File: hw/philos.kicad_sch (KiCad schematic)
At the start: 25 parts, among them SW2 Reset Button, U1 8086_Min_Mode, U11 71256SA25TPGI, U12 SN74LS161AN, U13 SN74AHC14N, U14 8259, U15 W27C512-45Z, U16 71256SA25TPGI, U17 8255, U18 MAX232N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

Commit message: hw: do some minor changes
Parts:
- removed R9: 1K ohm, symbol Device:R
- added RV1: R_Potentiometer, symbol Device:R_Potentiometer
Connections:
- net GND: now also RV1.1
- net VCC: now also RV1.3
- net indirizzi0: now also A2.D22; no longer A2.D2 (D2_INT0)
- net indirizzi1: now also A2.D23; no longer A2.D3 (D3_INT1)
- net indirizzi10: now also A2.D32; no longer A2.D12
- net indirizzi11: now also A2.D33; no longer A2.D13
- net indirizzi12: now also A2.D34; no longer A2.D22
- net indirizzi13: now also A2.D35; no longer A2.D23
- net indirizzi14: now also A2.D36; no longer A2.D24
- net indirizzi15: now also A2.D37; no longer A2.D25
- net indirizzi16: now also A2.D38; no longer A2.D26
- net indirizzi17: now also A2.D39; no longer A2.D27
- net indirizzi18: now also A2.D40; no longer A2.D28
- net indirizzi19: now also A2.D41; no longer A2.D29
- net indirizzi2: now also A2.D24; no longer A2.D4
- net indirizzi3: now also A2.D25; no longer A2.D5
- net indirizzi4: now also A2.D26; no longer A2.D6
- net indirizzi5: now also A2.D27; no longer A2.D7
- net indirizzi6: now also A2.D28; no longer A2.D8
- net indirizzi7: now also A2.D29; no longer A2.D9
- net indirizzi8: now also A2.D30; no longer A2.D10
- net indirizzi9: now also A2.D31; no longer A2.D11
- net at U5.20 (*CE): now also A2.D49; no longer A2.D37
- net at U14.1 (~{CS}): now also A2.D46; no longer A2.D34
- net at U11.20 (~{CS}), U16.20 (~{CS}): now also A2.D47; no longer A2.D35
- net at U1.28 (M/~{IO}): now also A2.D42; no longer A2.D30
- net at U7.11 (*CS): now also A2.D43; no longer A2.D31
- net at DS2.8 (E): now also A2.D44; no longer A2.D32
- net at U17.6 (~{CS}): now also A2.D45; no longer A2.D33
- net at U15.20 (*CE): now also A2.D48; no longer A2.D36
- net at DS2.5 (Vo): now also RV1.2

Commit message: hw: Add control bus pins on Arduino
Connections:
- net at U5.20 (*CE): now also A2.D52 (D52_SCK); no longer A2.D49
- net at U14.1 (~{CS}): now also A2.D49; no longer A2.D46
- net at U1.29 (~{WR}), U11.27 (~{WE}), U14.2 (~{WR})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: now also A2.D44
- net at U1.32 (~{RD}), U11.22 (~{OE}), U14.3 (~{RD})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: now also A2.D43
- net at U11.20 (~{CS}), U16.20 (~{CS}): now also A2.D50 (D50_MISO); no longer A2.D47
- net at A2.D42: now also U1.25 (ALE), U6.11 (LE), U8.11 (LE), U9.11 (LE); no longer U1.28 (M/~{IO})
- net at U7.11 (*CS): now also A2.D46; no longer A2.D43
- net at DS2.8 (E): now also A2.D47; no longer A2.D44
- net at A2.D45: now also U1.28 (M/~{IO}); no longer U17.6 (~{CS})
- net at A2.D48: now also U17.6 (~{CS}); no longer U15.20 (*CE)
- net at A2.D51 (D51_MOSI): now also U15.20 (*CE)

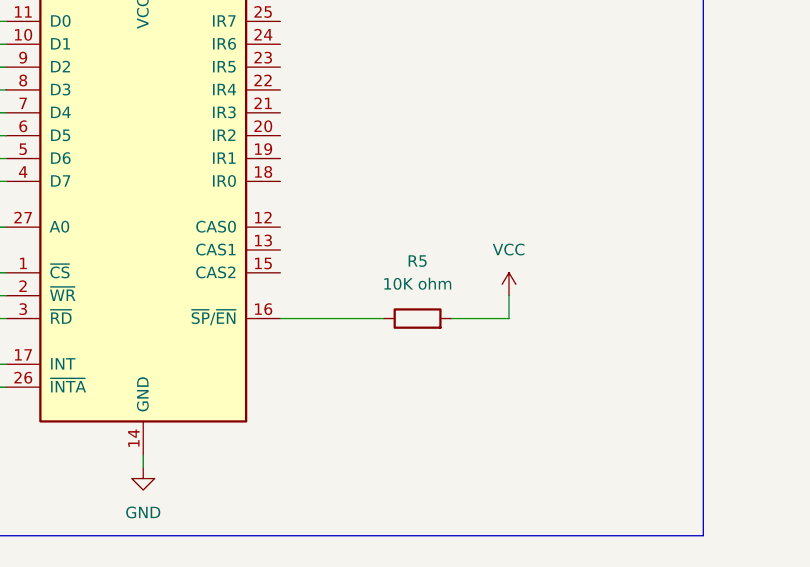
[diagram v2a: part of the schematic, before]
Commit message: hw: remove 1 resistor
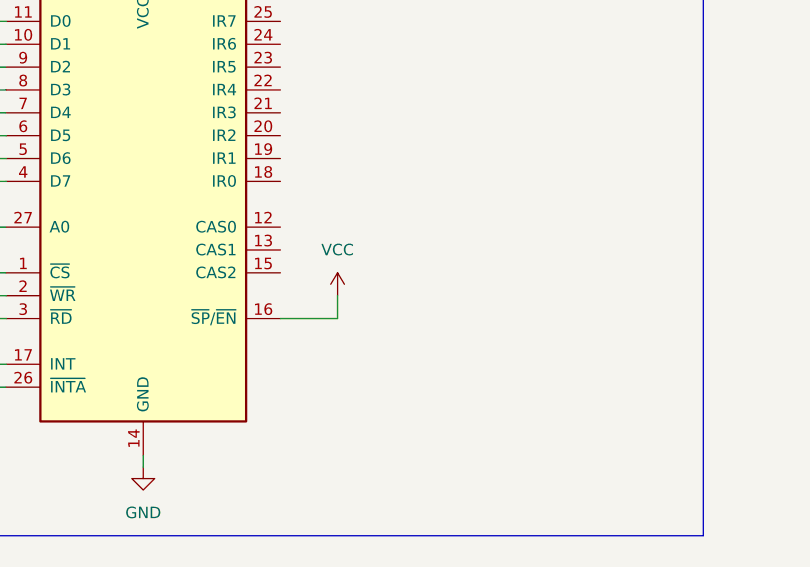
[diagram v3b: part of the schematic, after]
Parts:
- removed R5: 10K ohm, symbol Device:R
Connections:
- net VCC: now also U14.16 (~{SP}/~{EN})
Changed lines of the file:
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@@
 	(wire
 		(pts
-			(xy 410.21 523.24) (xy 416.56 523.24)
+			(xy 391.16 523.24) (xy 397.51 523.24)
 		)
 		(stroke
@@
 		)
 	)
-	(wire
-		(pts
-			(xy 391.16 523.24) (xy 402.59 523.24)
-		)
-		(stroke
-			(width 0)
-			(type default)
-		)
-	)
 	(bus
 		(pts
@@
 	(wire
 		(pts
-			(xy 416.56 523.24) (xy 416.56 520.7)
+			(xy 397.51 523.24) (xy 397.51 520.7)
 		)
 		(stroke
@@
 		(polyline
 			(pts
-				(xy 91.44 426.72) (xy 186.69 426.72) (xy 186.69 558.8) (xy 91.44 558.8) (xy 91.44 557.53)
+				(xy 325.12 468.63) (xy 325.12 557.53) (xy 425.45 557.53) (xy 425.45 468.63)
 			)
 			(stroke
@@
 		(polyline
 			(pts
-				(xy 452.12 408.94) (xy 452.12 562.61) (xy 581.66 562.61) (xy 581.66 408.94)
+				(xy 690.88 173.99) (xy 820.42 173.99) (xy 820.42 332.74) (xy 690.88 332.74) (xy 690.88 331.47)
 			)
 			(stroke
@@
 		(polyline
 			(pts
-				(xy 416.56 20.32) (xy 416.56 100.33) (xy 618.49 100.33) (xy 618.49 20.32)
+				(xy 669.29 41.91) (xy 669.29 114.3) (xy 749.3 114.3) (xy 749.3 41.91)
 			)
 			(stroke
@@
 		(polyline
 			(pts
-				(xy 325.12 468.63) (xy 325.12 557.53) (xy 425.45 557.53) (xy 425.45 468.63)
+				(xy 49.53 34.29) (xy 49.53 201.93) (xy 194.31 201.93) (xy 198.12 201.93) (xy 198.12 34.29)
 			)
 			(stroke
@@
 		(polyline
 			(pts
-				(xy 49.53 34.29) (xy 49.53 201.93) (xy 194.31 201.93) (xy 198.12 201.93) (xy 198.12 34.29)
+				(xy 655.32 361.95) (xy 821.69 361.95) (xy 821.69 482.6) (xy 821.69 483.87) (xy 655.32 483.87) (xy 655.32 482.6)
 			)
 			(stroke
@@
 		(polyline
 			(pts
-				(xy 690.88 173.99) (xy 820.42 173.99) (xy 820.42 332.74) (xy 690.88 332.74) (xy 690.88 331.47)
+				(xy 452.12 408.94) (xy 452.12 562.61) (xy 581.66 562.61) (xy 581.66 408.94)
 			)
 			(stroke
@@
 		(polyline
 			(pts
-				(xy 655.32 361.95) (xy 821.69 361.95) (xy 821.69 482.6) (xy 821.69 483.87) (xy 655.32 483.87) (xy 655.32 482.6)
+				(xy 22.86 234.95) (xy 22.86 378.46) (xy 175.26 378.46) (xy 175.26 234.95)
 			)
 			(stroke
@@
 		(polyline
 			(pts
-				(xy 669.29 41.91) (xy 669.29 114.3) (xy 749.3 114.3) (xy 749.3 41.91)
+				(xy 267.97 60.96) (xy 267.97 102.87) (xy 332.74 102.87) (xy 332.74 62.23) (xy 332.74 60.96)
 			)
 			(stroke
@@
 		(polyline
 			(pts
-				(xy 267.97 60.96) (xy 267.97 102.87) (xy 332.74 102.87) (xy 332.74 62.23) (xy 332.74 60.96)
+				(xy 416.56 20.32) (xy 416.56 100.33) (xy 618.49 100.33) (xy 618.49 20.32)
 			)
 			(stroke
@@
 		(polyline
 			(pts
-				(xy 22.86 234.95) (xy 22.86 378.46) (xy 175.26 378.46) (xy 175.26 234.95)
+				(xy 91.44 426.72) (xy 186.69 426.72) (xy 186.69 558.8) (xy 91.44 558.8) (xy 91.44 557.53)
 			)
 			(stroke
@@
 	)
 	(symbol
-		(lib_id "Device:R")
-		(at 406.4 523.24 90)
-		(unit 1)
-		(exclude_from_sim no)
-		(in_bom yes)
-		(on_board yes)
-		(dnp no)
-		(fields_autoplaced yes)
-		(property "Reference" "R5"
-			(at 406.4 516.89 90)
-			(effects
-				(font
-					(size 1.27 1.27)
-				)
-			)
-		)
-		(property "Value" "10K ohm"
-			(at 406.4 519.43 90)
-			(effects
-				(font
-					(size 1.27 1.27)
-				)
-			)
-		)
-		(property "Footprint" ""
-			(at 406.4 525.018 90)
-			(effects
-				(font
-					(size 1.27 1.27)
-				)
-				(hide yes)
-			)
-		)
-		(property "Datasheet" "~"
-			(at 406.4 523.24 0)
-			(effects
-				(font
-					(size 1.27 1.27)
-				)
-				(hide yes)
-			)
-		)
-		(property "Description" "Resistor"
-			(at 406.4 523.24 0)
-			(effects
-				(font
-					(size 1.27 1.27)
-				)
-				(hide yes)
-			)
-		)
-		(pin "1"
-		)
-		(pin "2"
-		)
-		(instances
-			(project "philos"
-				(path "/0711ae6c-3a16-437c-9df1-9f60cb60f958"
-					(reference "R5")
-					(unit 1)
-				)
-			)
-		)
-	)
-	(symbol
 		(lib_id "power:VCC")
 		(at 154.94 260.35 0)
@@
 	(symbol
 		(lib_id "power:VCC")
-		(at 416.56 520.7 0)
+		(at 397.51 520.7 0)
 		(unit 1)
 		(exclude_from_sim no)
@@
 		(fields_autoplaced yes)
 		(property "Reference" "#PWR055"
-			(at 416.56 524.51 0)
+			(at 397.51 524.51 0)
 			(effects
 				(font
@@
 		)
 		(property "Value" "VCC"
-			(at 416.56 515.62 0)
+			(at 397.51 515.62 0)
 			(effects
 				(font
@@
 		)
 		(property "Footprint" ""
-			(at 416.56 520.7 0)
+			(at 397.51 520.7 0)
 			(effects
 				(font
@@
 		)
 		(property "Datasheet" ""
-			(at 416.56 520.7 0)
+			(at 397.51 520.7 0)
 			(effects
 				(font
@@
 		)
 		(property "Description" "Power symbol creates a global label with name \"VCC\""
-			(at 416.56 520.7 0)
+			(at 397.51 520.7 0)
 			(effects
 				(font

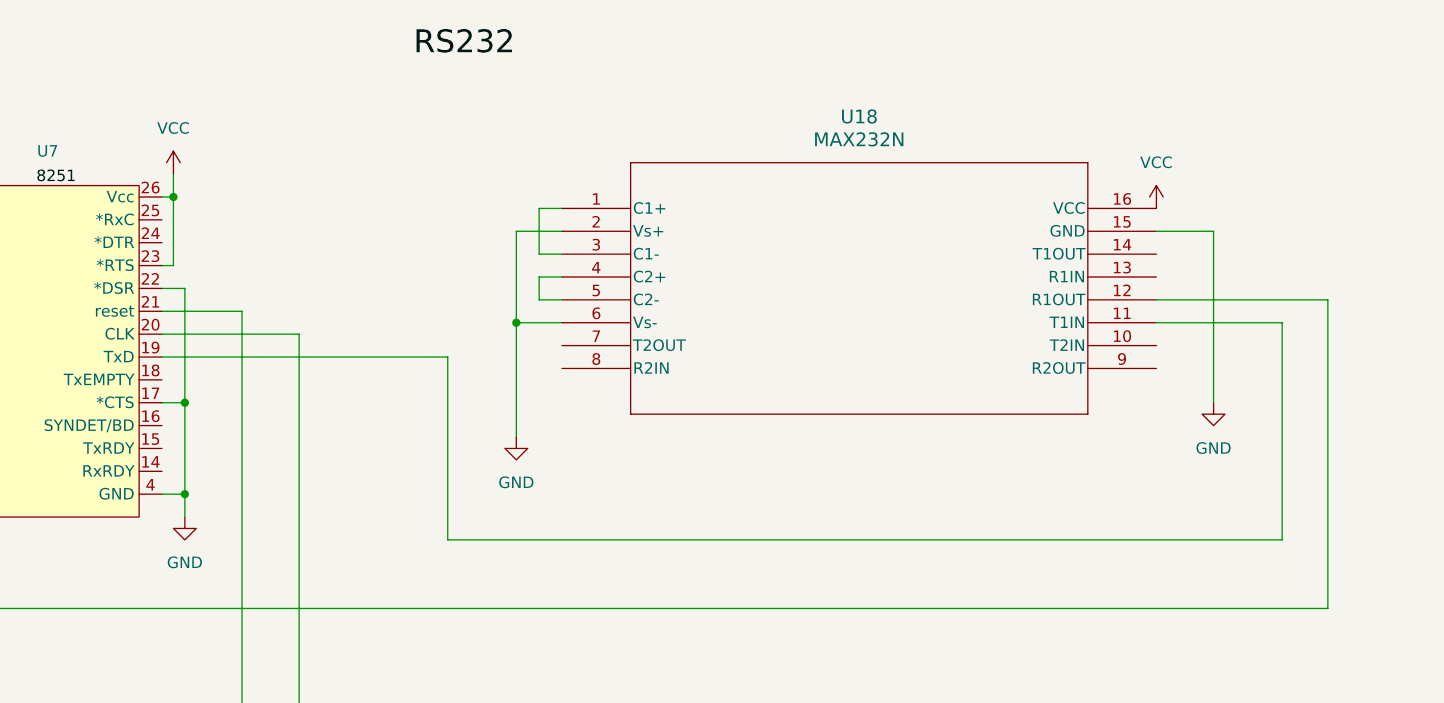
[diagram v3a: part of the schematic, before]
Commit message: hw: add capacitors to max232
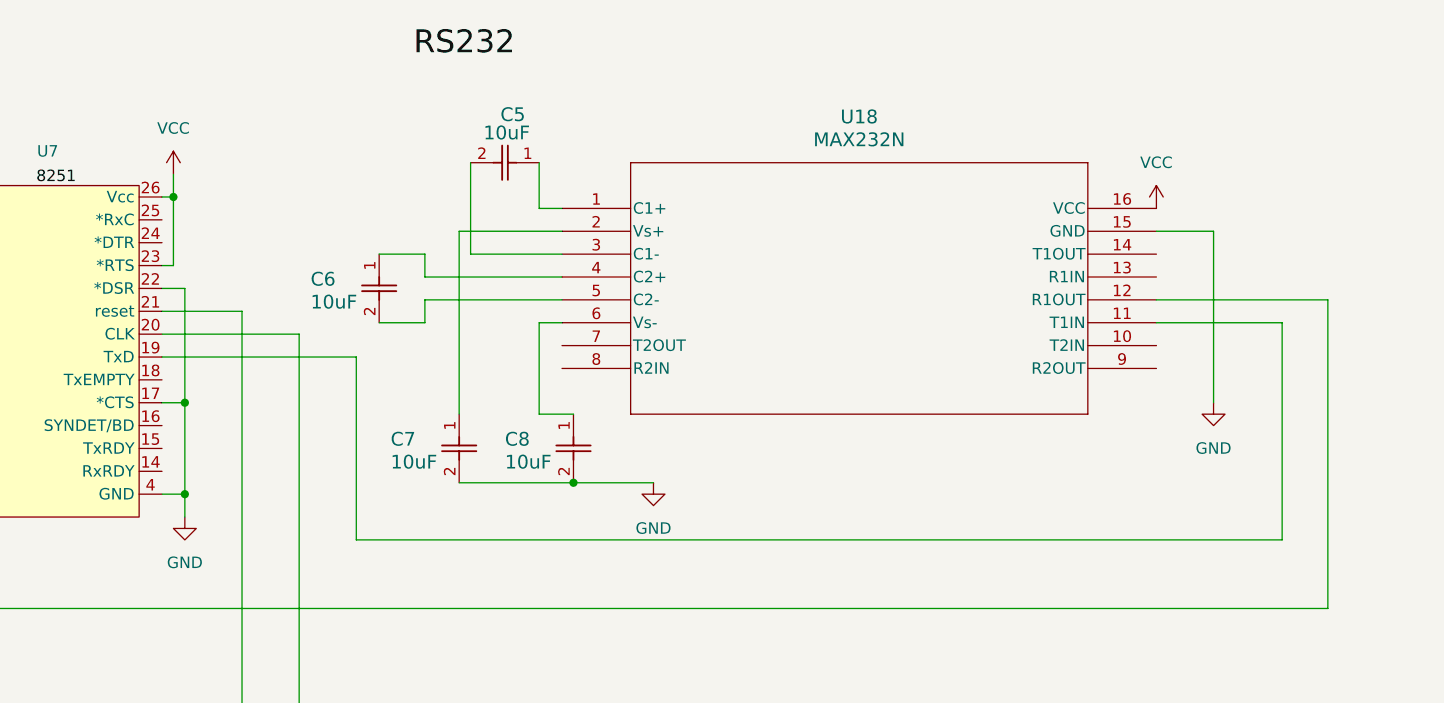
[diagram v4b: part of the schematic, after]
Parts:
- added C5, C6, C7, C8: 10uF, K150J15C0GF5TL2_VIS, symbol K150J15C0GF5TL2:K150J15C0GF5TL2
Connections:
- net GND: now also C7.2, C8.2; no longer U18.2 (Vs+), U18.6 (Vs-)
- net at U18.1 (C1+): now also C5.1; no longer U18.3 (C1-)
- net at U18.4 (C2+): now also C6.1; no longer U18.5 (C2-)
- new net: C7.1, U18.2 (Vs+)
- new net: C5.2, U18.3 (C1-)
- new net: C6.2, U18.5 (C2-)
- new net: C8.1, U18.6 (Vs-)

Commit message: hw: updated schematic
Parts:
- removed A2: Arduino_Mega2560_R3_Shield, PCM_arduino-library:Arduino_Mega2560_R3_Shield, symbol Arduino:Arduino_Mega2560_R3_Shield
- added R9: 10K ohm, symbol Device:R
- added U19, U20: SN74LS161AN, N16, symbol SN74LS161AN:SN74LS161AN
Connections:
- net GND: now also U19.3 (A), U19.4 (B), U19.5 (C), U19.6 (D), U19.8 (GND), U20.3 (A), U20.4 (B), U20.5 (C), U20.6 (D), U20.8 (GND)
- net VCC: now also R9.2, U19.1 (*CLR), U19.10 (ENT), U19.16 (VCC), U19.7 (ENP), U19.9 (*LOAD), U20.1 (*CLR), U20.10 (ENT), U20.16 (VCC), U20.7 (ENP), U20.9 (*LOAD); no longer U14.16 (~{SP}/~{EN})
- net indirizzi0: no longer U15.10 (A0), U5.10 (A0)
- net indirizzi1: now also U15.10 (A0), U5.10 (A0); no longer U15.9 (A1), U5.9 (A1)
- net indirizzi10: now also U15.24 (A9), U5.24 (A9); no longer U15.21 (A10), U5.21 (A10)
- net indirizzi11: now also U15.21 (A10), U5.21 (A10); no longer U15.23 (A11), U5.23 (A11)
- net indirizzi12: now also U15.23 (A11), U5.23 (A11); no longer U15.2 (A12), U5.2 (A12)
- net indirizzi13: now also U15.2 (A12), U5.2 (A12); no longer U15.26 (A13), U5.26 (A13)
- net indirizzi14: now also U15.26 (A13), U5.26 (A13); no longer U15.27 (A14), U5.27 (A14)
- net indirizzi15: now also U15.27 (A14), U5.27 (A14); no longer U15.1 (A15), U5.1 (A15)
- net indirizzi16: now also U15.1 (A15), U5.1 (A15)
- net indirizzi2: now also U15.9 (A1), U5.9 (A1); no longer U15.8 (A2), U5.8 (A2)
- net indirizzi3: now also U15.8 (A2), U5.8 (A2); no longer U15.7 (A3), U5.7 (A3)
- net indirizzi4: now also U15.7 (A3), U5.7 (A3); no longer U15.6 (A4), U5.6 (A4)
- net indirizzi5: now also U15.6 (A4), U5.6 (A4); no longer U15.5 (A5), U5.5 (A5)
- net indirizzi6: now also U15.5 (A5), U5.5 (A5); no longer U15.4 (A6), U5.4 (A6)
- net indirizzi7: now also U15.4 (A6), U5.4 (A6); no longer U15.3 (A7), U5.3 (A7)
- net indirizzi8: now also U15.3 (A7), U5.3 (A7); no longer U15.25 (A8), U5.25 (A8)
- net indirizzi9: now also U15.25 (A8), U5.25 (A8); no longer U15.24 (A9), U5.24 (A9)
- net at U5.20 (*CE): now also U15.20 (*CE)
- net at U13.10 (5Y): now also U19.2 (CLK)
- net at U13.11 (5A): now also U12.12 (QC)
- net at U13.12 (6Y): now also U12.2 (CLK)
- net at U13.13 (6A): now also U20.12 (QC)
- net at R4.2, R7.1, U13.2 (1Y): now also U20.2 (CLK); no longer U12.2 (CLK)
- net at U13.8 (4Y): now also U1.19 (CLK), U7.20 (CLK)
- net at U13.9 (4A): now also U19.12 (QC)
- net at U12.11 (QD): no longer U7.20 (CLK)
- net at U12.14 (QA): no longer U1.19 (CLK)
- new net: R9.1, U14.16 (~{SP}/~{EN})
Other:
- moved on the sheet: C3, C4, R4, R7, U12, U13, Y2
